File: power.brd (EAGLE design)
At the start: 90.2 x 95.9 mm, 65 parts, among them J1 POWER_JACKPTH_BREAD, T1 SINGLE_NCHAN_FET, T2 SINGLE_NCHAN_FET, T3 SINGLE_NCHAN_FET, U1 MOSFET_PCHAN_20A, U14 MOSFET_PCHAN_20A, U2 MOSFET_PCHAN_20A

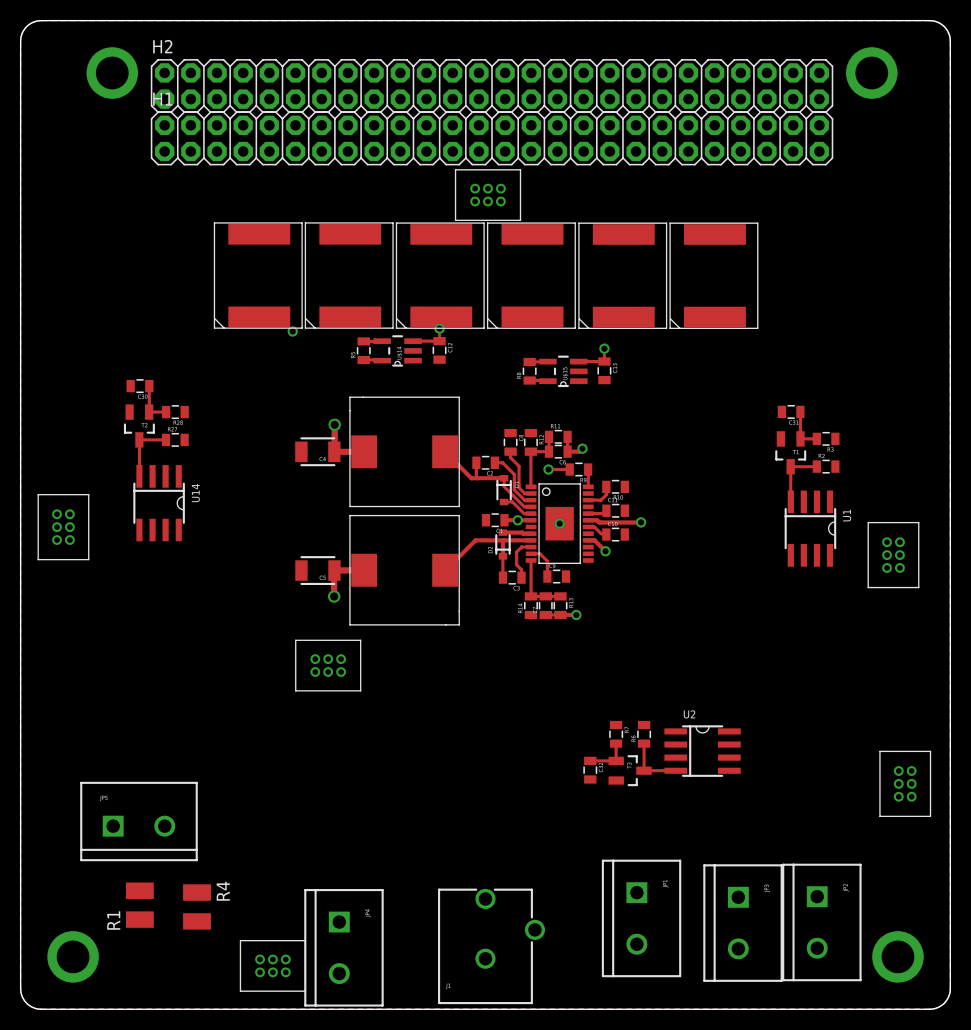
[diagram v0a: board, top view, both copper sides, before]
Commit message: Updated Gecko Connector
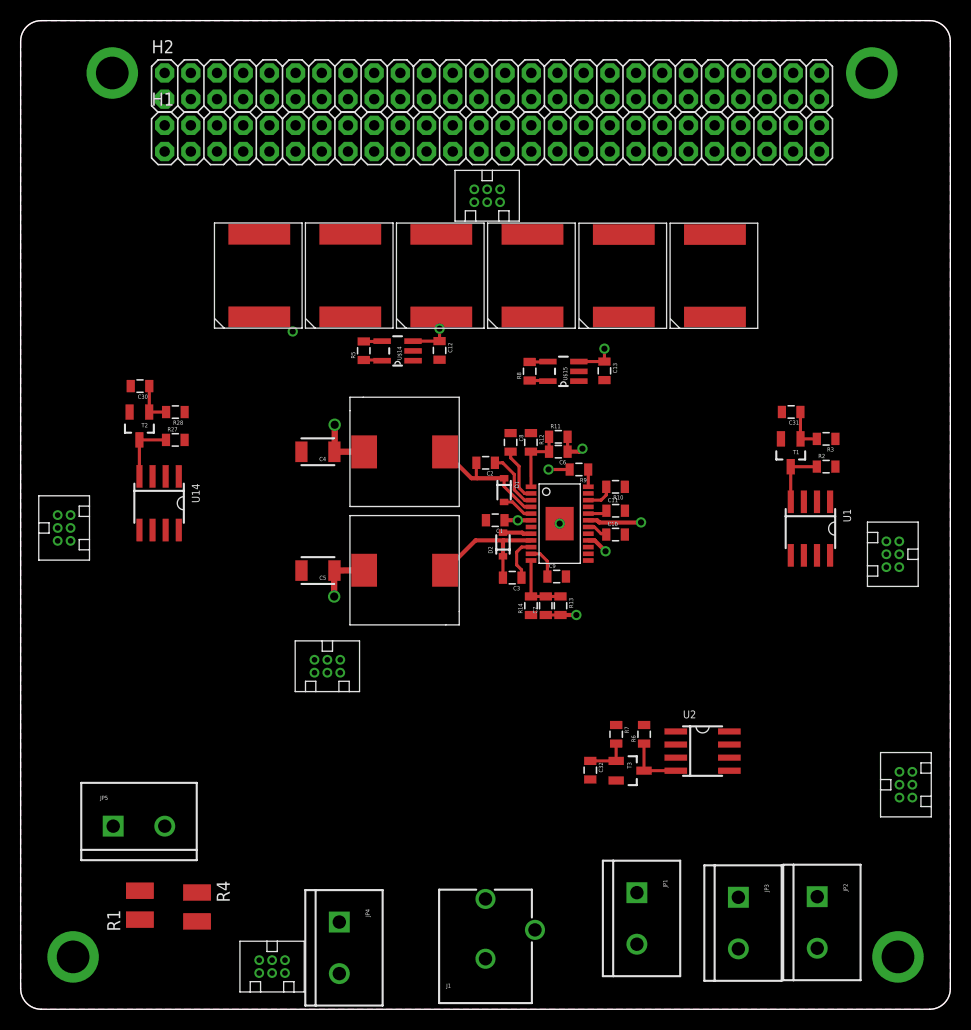
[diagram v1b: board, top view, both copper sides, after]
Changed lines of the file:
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@@
 <contactref element="U$6" pad="P2"/>
 <contactref element="U$6" pad="P5"/>
-<wire x1="4.78" y1="46.76" x2="3.53" y2="46.76" width="0" layer="19" extent="1-1"/>
-<wire x1="15.335" y1="46.48" x2="4.78" y2="46.76" width="0" layer="19" extent="1-1"/>
+<wire x1="4.845" y1="46.68" x2="3.595" y2="46.68" width="0" layer="19" extent="1-1"/>
+<wire x1="15.335" y1="46.48" x2="4.845" y2="46.68" width="0" layer="19" extent="1-1"/>
 <wire x1="14.065" y1="46.48" x2="15.335" y2="46.48" width="0" layer="19" extent="1-1"/>
 <wire x1="12.795" y1="46.48" x2="14.065" y2="46.48" width="0" layer="19" extent="1-1"/>
@@
 <wire x1="75.965" y1="44.02" x2="77.235" y2="44.02" width="0" layer="19" extent="1-1"/>
 <wire x1="74.695" y1="44.02" x2="75.965" y2="44.02" width="0" layer="19" extent="1-1"/>
-<wire x1="84.03" y1="44.05" x2="78.505" y2="44.02" width="0" layer="19" extent="1-1"/>
-<wire x1="85.28" y1="44.05" x2="84.03" y2="44.05" width="0" layer="19" extent="1-1"/>
+<wire x1="83.965" y1="44.13" x2="78.505" y2="44.02" width="0" layer="19" extent="1-1"/>
+<wire x1="85.215" y1="44.13" x2="83.965" y2="44.13" width="0" layer="19" extent="1-1"/>
 </signal>
 <signal name="N$2">
@@
 <contactref element="U$3" pad="P3"/>
 <contactref element="U$3" pad="P6"/>
-<wire x1="46.58" y1="78.34" x2="46.58" y2="79.59" width="0" layer="19" extent="1-1"/>
-<wire x1="35.0599" y1="64.8" x2="46.58" y2="78.34" width="0" layer="19" extent="1-1"/>
-<wire x1="31.08" y1="33.96" x2="33.28" y2="64.77" width="0" layer="19" extent="1-1"/>
-<wire x1="31.08" y1="32.71" x2="31.08" y2="33.96" width="0" layer="19" extent="1-1"/>
-<wire x1="25.72" y1="4.83" x2="31.08" y2="32.71" width="0" layer="19" extent="1-1"/>
-<wire x1="25.72" y1="3.58" x2="25.72" y2="4.83" width="0" layer="19" extent="1-1"/>
-<wire x1="4.78" y1="48.01" x2="31.08" y2="33.96" width="0" layer="19" extent="1-1"/>
-<wire x1="3.53" y1="48.01" x2="4.78" y2="48.01" width="0" layer="19" extent="1-1"/>
-<wire x1="84.03" y1="42.8" x2="46.58" y2="78.34" width="0" layer="19" extent="1-1"/>
-<wire x1="85.28" y1="42.8" x2="84.03" y2="42.8" width="0" layer="19" extent="1-1"/>
-<wire x1="85.17" y1="23.11" x2="85.28" y2="42.8" width="0" layer="19" extent="1-1"/>
-<wire x1="86.42" y1="23.11" x2="85.17" y2="23.11" width="0" layer="19" extent="1-1"/>
+<wire x1="46.5" y1="78.275" x2="46.5" y2="79.525" width="0" layer="19" extent="1-1"/>
+<wire x1="35.0599" y1="64.8" x2="46.5" y2="78.275" width="0" layer="19" extent="1-1"/>
+<wire x1="31" y1="33.895" x2="33.28" y2="64.77" width="0" layer="19" extent="1-1"/>
+<wire x1="31" y1="32.645" x2="31" y2="33.895" width="0" layer="19" extent="1-1"/>
+<wire x1="25.64" y1="4.765" x2="31" y2="32.645" width="0" layer="19" extent="1-1"/>
+<wire x1="25.64" y1="3.515" x2="25.64" y2="4.765" width="0" layer="19" extent="1-1"/>
+<wire x1="4.845" y1="47.93" x2="31" y2="33.895" width="0" layer="19" extent="1-1"/>
+<wire x1="3.595" y1="47.93" x2="4.845" y2="47.93" width="0" layer="19" extent="1-1"/>
+<wire x1="83.965" y1="42.88" x2="46.5" y2="78.275" width="0" layer="19" extent="1-1"/>
+<wire x1="85.215" y1="42.88" x2="83.965" y2="42.88" width="0" layer="19" extent="1-1"/>
+<wire x1="85.235" y1="23.03" x2="85.215" y2="42.88" width="0" layer="19" extent="1-1"/>
+<wire x1="86.485" y1="23.03" x2="85.235" y2="23.03" width="0" layer="19" extent="1-1"/>
 </signal>
 <signal name="N$7">

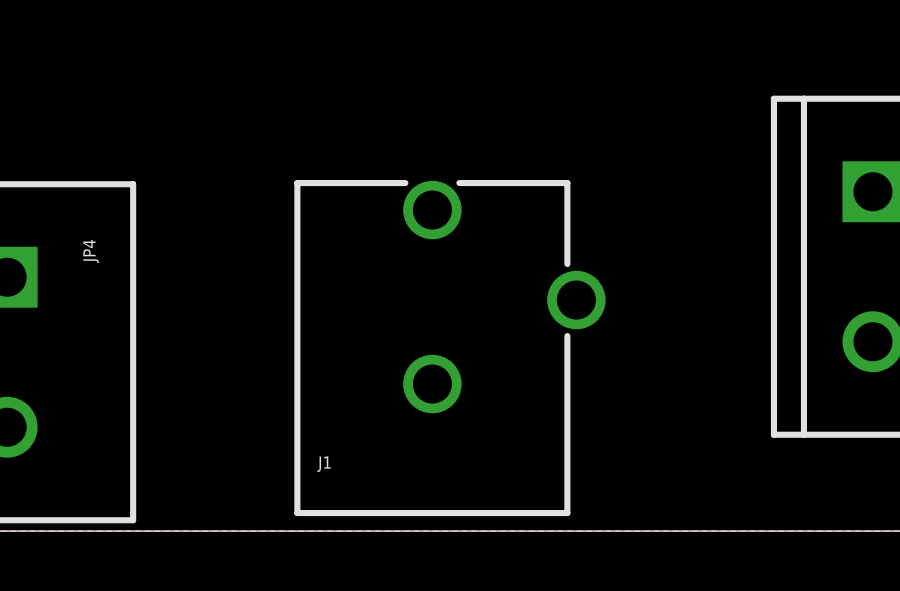
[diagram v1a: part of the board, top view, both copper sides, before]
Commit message: Switching to teensy for flight computer
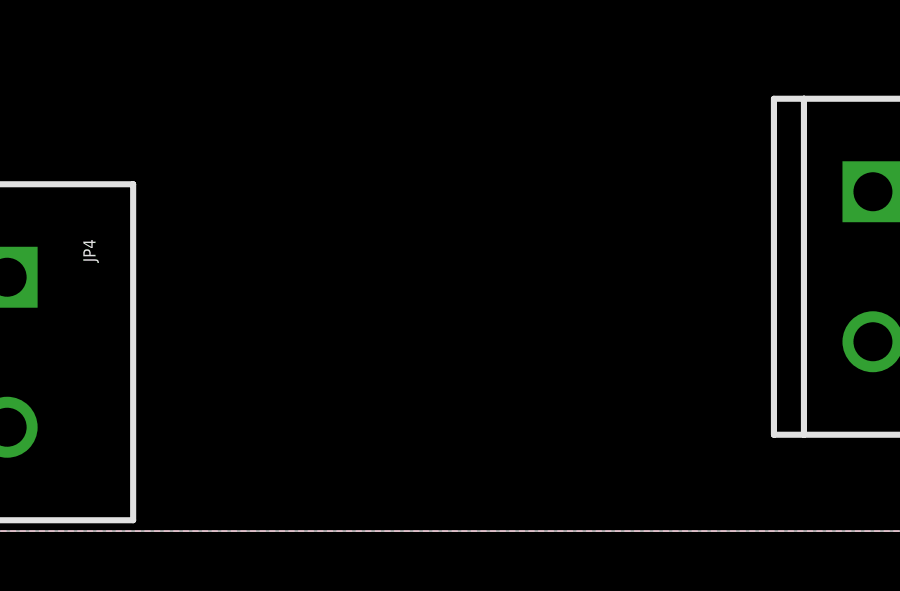
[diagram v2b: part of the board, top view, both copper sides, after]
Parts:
- removed J1: POWER_JACKPTH_BREAD, SparkFun-Connectors:POWER_JACK_PTH_BREAD
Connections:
- net BATT_INPUT: no longer J1.PWR
- net GND: no longer J1.GND, J1.GNDBREAK
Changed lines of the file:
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@@
 <element name="U$11" library="Widetronix" package="BETABATTERY" value="BETABATTERY" x="58.4" y="71.14" rot="R90"/>
 <element name="U$12" library="Widetronix" package="BETABATTERY" value="BETABATTERY" x="67.24" y="71.14" rot="R90"/>
-<element name="J1" library="SparkFun-Connectors" package="POWER_JACK_PTH_BREAD" value="POWER_JACKPTH_BREAD" x="45.085" y="-3">
-<attribute name="PROD_ID" value="PRT-10811" x="45.085" y="-3" size="1.778" layer="27" display="off"/>
-</element>
 <element name="JP1" library="SparkFun-Connectors" package="SCREWTERMINAL-5MM-2" value="M025MM" x="59.77" y="11.31" rot="R270"/>
 <element name="JP2" library="SparkFun-Connectors" package="SCREWTERMINAL-5MM-2" value="M025MM" x="77.26" y="10.92" rot="R270"/>
@@
 <contactref element="U$11" pad="V-"/>
 <contactref element="U$12" pad="V-"/>
-<contactref element="J1" pad="GND"/>
-<contactref element="J1" pad="GNDBREAK"/>
 <contactref element="JP1" pad="1"/>
 <contactref element="JP2" pad="1"/>
@@
 <via x="26.39" y="65.74" extent="1-16" drill="0.6"/>
 <via x="52.28" y="47.1" extent="1-16" drill="0.6"/>
+<wire x1="67.34" y1="75.14" x2="82.55" y2="90.805" width="0" layer="19" extent="1-1"/>
+<wire x1="58.5" y1="75.14" x2="67.34" y2="75.14" width="0" layer="19" extent="1-1"/>
+<wire x1="49.64" y1="75.15" x2="58.5" y2="75.14" width="0" layer="19" extent="1-1"/>
+<wire x1="44" y1="78.275" x2="49.64" y2="75.15" width="0" layer="19" extent="1-1"/>
+<wire x1="44" y1="79.525" x2="44" y2="78.275" width="0" layer="19" extent="1-1"/>
+<wire x1="40.8" y1="75.15" x2="44" y2="78.275" width="0" layer="19" extent="1-1"/>
+<wire x1="31.97" y1="75.16" x2="40.8" y2="75.15" width="0" layer="19" extent="1-1"/>
+<wire x1="23.15" y1="75.16" x2="31.97" y2="75.16" width="0" layer="19" extent="1-1"/>
+<wire x1="26.39" y1="65.74" x2="23.15" y2="75.16" width="0" layer="19" extent="1-1"/>
+<wire x1="49.53" y1="88.27" x2="44" y2="79.525" width="0" layer="19" extent="1-1"/>
+<wire x1="52.07" y1="88.27" x2="49.53" y2="88.27" width="0" layer="19" extent="1-1"/>
+<wire x1="52.07" y1="90.81" x2="52.07" y2="88.27" width="0" layer="19" extent="1-1"/>
+<wire x1="49.53" y1="90.81" x2="49.53" y2="88.27" width="0" layer="19" extent="1-1"/>
+<wire x1="27.23" y1="54.07" x2="26.39" y2="65.74" width="0" layer="19" extent="1-1"/>
+<wire x1="27.24" y1="42.55" x2="27.23" y2="54.07" width="0" layer="19" extent="1-1"/>
+<wire x1="28.5" y1="33.895" x2="27.24" y2="42.55" width="0" layer="19" extent="1-1"/>
+<wire x1="28.5" y1="32.645" x2="28.5" y2="33.895" width="0" layer="19" extent="1-1"/>
+<wire x1="38.0601" y1="62.9" x2="26.39" y2="65.74" width="0" layer="19" extent="1-1"/>
+<wire x1="40.63" y1="63" x2="38.0601" y2="62.9" width="0" layer="19" extent="1-1"/>
+<wire x1="47.52" y1="55.88" x2="40.63" y2="63" width="0" layer="19" extent="1-1"/>
+<wire x1="49.49" y1="55.88" x2="47.52" y2="55.88" width="0" layer="19" extent="1-1"/>
+<wire x1="54.1401" y1="60.92" x2="49.49" y2="55.88" width="0" layer="19" extent="1-1"/>
+<wire x1="56.62" y1="61.02" x2="54.1401" y2="60.92" width="0" layer="19" extent="1-1"/>
+<wire x1="55.055" y1="50.025" x2="49.49" y2="55.88" width="0" layer="19" extent="1-1"/>
+<wire x1="58.6" y1="50.67" x2="55.055" y2="50.025" width="0" layer="19" extent="1-1"/>
+<wire x1="58.61" y1="48.35" x2="58.6" y2="50.67" width="0" layer="19" extent="1-1"/>
+<wire x1="58.6" y1="46.04" x2="58.61" y2="48.35" width="0" layer="19" extent="1-1"/>
+<wire x1="52.28" y1="47.1" x2="55.055" y2="50.025" width="0" layer="19" extent="1-1"/>
+<wire x1="52.89" y1="41.97" x2="52.28" y2="47.1" width="0" layer="19" extent="1-1"/>
+<wire x1="49.5" y1="38.24" x2="52.89" y2="41.97" width="0" layer="19" extent="1-1"/>
+<wire x1="45.13" y1="47.43" x2="52.28" y2="47.1" width="0" layer="19" extent="1-1"/>
+<wire x1="73.74" y1="55.32" x2="58.6" y2="50.67" width="0" layer="19" extent="1-1"/>
+<wire x1="73.83" y1="57.93" x2="73.74" y2="55.32" width="0" layer="19" extent="1-1"/>
+<wire x1="83.965" y1="45.38" x2="73.74" y2="55.32" width="0" layer="19" extent="1-1"/>
+<wire x1="85.215" y1="45.38" x2="83.965" y2="45.38" width="0" layer="19" extent="1-1"/>
+<wire x1="10.68" y1="60.44" x2="26.39" y2="65.74" width="0" layer="19" extent="1-1"/>
+<wire x1="10.57" y1="57.92" x2="10.68" y2="60.44" width="0" layer="19" extent="1-1"/>
+<wire x1="4.845" y1="45.43" x2="10.57" y2="57.92" width="0" layer="19" extent="1-1"/>
+<wire x1="3.595" y1="45.43" x2="4.845" y2="45.43" width="0" layer="19" extent="1-1"/>
+<wire x1="55.25" y1="22.29" x2="49.5" y2="38.24" width="0" layer="19" extent="1-1"/>
+<wire x1="57.76" y1="22.19" x2="55.25" y2="22.29" width="0" layer="19" extent="1-1"/>
+<wire x1="59.77" y1="11.31" x2="57.76" y2="22.19" width="0" layer="19" extent="1-1"/>
+<wire x1="69.61" y1="10.86" x2="59.77" y2="11.31" width="0" layer="19" extent="1-1"/>
+<wire x1="77.26" y1="10.92" x2="69.61" y2="10.86" width="0" layer="19" extent="1-1"/>
+<wire x1="85.09" y1="5.08" x2="77.26" y2="10.92" width="0" layer="19" extent="1-1"/>
+<wire x1="85.235" y1="20.53" x2="77.26" y2="10.92" width="0" layer="19" extent="1-1"/>
+<wire x1="86.485" y1="20.53" x2="85.235" y2="20.53" width="0" layer="19" extent="1-1"/>
+<wire x1="8.89" y1="90.805" x2="23.15" y2="75.16" width="0" layer="19" extent="1-1"/>
+<wire x1="23.14" y1="4.765" x2="28.5" y2="32.645" width="0" layer="19" extent="1-1"/>
+<wire x1="23.14" y1="3.515" x2="23.14" y2="4.765" width="0" layer="19" extent="1-1"/>
+<wire x1="5.09" y1="5.08" x2="23.14" y2="4.765" width="0" layer="19" extent="1-1"/>
 </signal>
 <signal name="VBACKUP">
@@
 <contactref element="JP4" pad="2"/>
 <contactref element="R1" pad="1"/>
-<contactref element="J1" pad="PWR"/>
-<wire x1="30.91" y1="3.46" x2="77.26" y2="5.92" width="0" layer="19" extent="1-1"/>
+<wire x1="59.77" y1="6.31" x2="77.26" y2="5.92" width="0" layer="19" extent="1-1"/>
+<wire x1="30.91" y1="3.46" x2="59.77" y2="6.31" width="0" layer="19" extent="1-1"/>
 <wire x1="11.57" y1="8.7" x2="30.91" y2="3.46" width="0" layer="19" extent="1-1"/>
-<wire x1="59.77" y1="6.31" x2="30.91" y2="3.46" width="0" layer="19" extent="1-1"/>
-<wire x1="45.085" y1="10.7" x2="59.77" y2="6.31" width="0" layer="19" extent="1-1"/>
 </signal>
 <signal name="ENAB_BURN2">
